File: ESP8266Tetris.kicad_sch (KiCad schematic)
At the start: 50 parts, among them J1 10118192-0001LF, Q1 BC847BLT1G, U2 STNS01PUR, U3 ESP-12F, U4 CH340G

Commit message: Battery charge and 3.3V LDO circuits changed, new datasheets added.
Signed-off-by: Ion Bold <bold.ion86@gmail.com>
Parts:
- removed C? (x3): 1u, symbol Device:C_Small
- removed C?: 2u2, symbol Device:C_Small
- removed C?: 4u7, symbol Device:C_Small
- removed R?: 10k, symbol Device:R_Small
- removed R?: 3M3?, symbol Device:R_Small
- removed R?: 10M?, symbol Device:R_Small
- removed U2: STNS01PUR, KiCadCustom:DFN12L_3x3mm_P0.45_EP2.12x1.31mm, symbol KiCadCustom:STNS01
- removed U?: BU33SD5WG-TR, Package_TO_SOT_SMD:SOT-23-5_HandSoldering, symbol KiCadCustom:BU33SD5WG-TR
- added C?: 1u, symbol Device:C_Small
- added C? (x2): 10u, symbol Device:C_Polarized_Small
- added R? (x2): 10k, symbol Device:R_Small
- added R?: 470R, symbol Device:R_Small
- added U?: LP3874EMPX-3.3/NOPB, Package_TO_SOT_SMD:SOT-223-5, symbol KiCadCustom:LP3874
- added U?: BQ25170, Package_SON:WSON-8-1EP_2x2mm_P0.5mm_EP0.9x1.6mm_ThermalVias, symbol KiCadCustom:BQ25170
- C1: value 2u2 -> 1u
- R1: value 1k -> 27k
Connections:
- net LED_EN is gone; now on net ROTATE: R?.2, U3.16 (GPIO15)
- net +3V3: now also C?.1, C?.2, Q?.2 (S), R?.1, R?.1, R?.1, R?.1, R?.1, U3.8 (VCC), C?.1, U?.3 (OUT), U?.4 (SENSE)
- net +5V: now also D?.2 (A), R?.2, U?.1 (IN)
- net BAT: now also BT?.1 (+), C?.1, C?.1, U?.2 (IN), U?.8 (OUT)
- net GND: now also C?.2, C?.2, C?.2, R?.2, R?.2, U?.4 (GND), U?.5 (GND)
- net ROTATE: no longer R?.2, U3.17 (GPIO2)
- net SD: now also R?.2, U3.17 (GPIO2), U?.1 (~{SD})
- net at R1.1: now also U?.7 (VSET)
- removed net +3V0: C?.1, C?.2, D?.2 (A), Q?.2 (S), R?.1, R?.1, R?.1, R?.1, R?.1, U3.8 (VCC)
- net LED_CHG: no longer names the net of R?.1
- net LED_CHG: now also U?.5 (STAT)
- new net: R?.1, U?.6 (~{PG})
- new net: R?.1, U?.2 (ISET)
- new net: R?.1, U?.3 (TS)
- no-connect marks 13 -> 12
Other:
- note added: "Condensatori tantal!!"
- note added: "PullDown resistors on buttons??"
- moved on the sheet: BT?, C1, D?, R1, R?

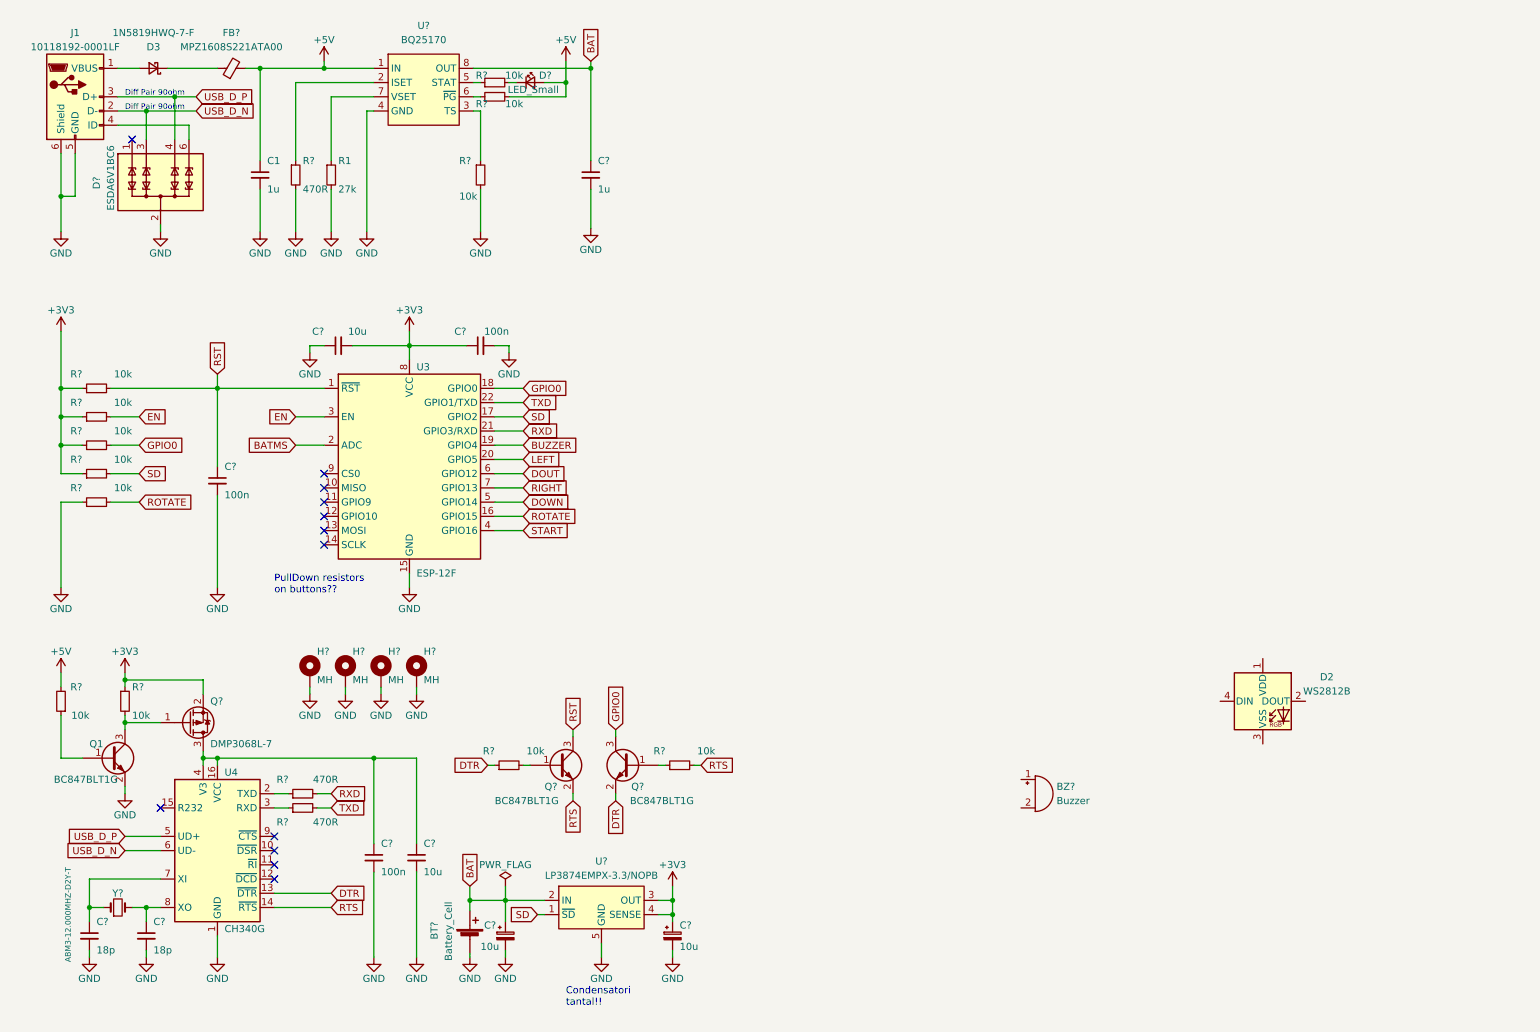
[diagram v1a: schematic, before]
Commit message: LEDs added to schematic, footprints assigned, PCB layout started.
Signed-off-by: Ion Bold <bold.ion86@gmail.com>
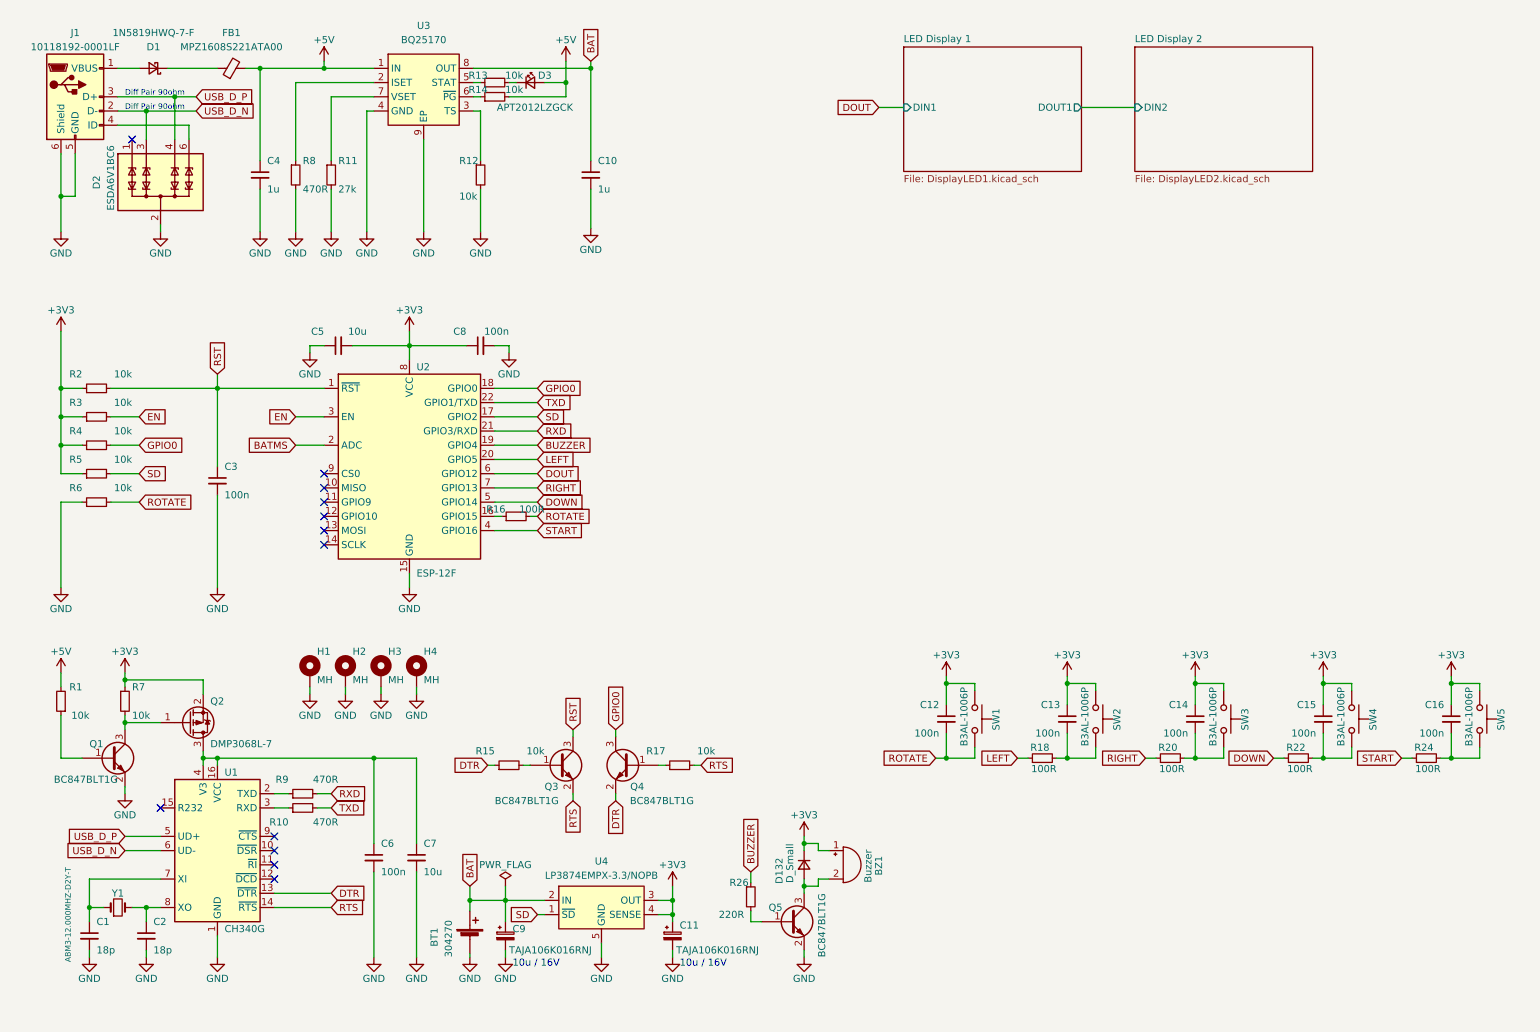
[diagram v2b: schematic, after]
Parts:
- removed D2: WS2812B, LED_SMD:LED_WS2812B_PLCC4_5.0x5.0mm_P3.2mm, symbol LED:WS2812B
- added C12, C13, C14, C15, C16: 100n, Capacitor_SMD:C_0603_1608Metric_Pad1.08x0.95mm_HandSolder, symbol Device:C_Small
- added D132: D_Small, Diode_SMD:D_MiniMELF, symbol Device:D_Small
- added Q5: BC847BLT1G, Package_TO_SOT_SMD:SOT-23, symbol Transistor_BJT:BC847
- added R16, R18, R20, R22, R24: 100R, Resistor_SMD:R_0603_1608Metric_Pad0.98x0.95mm_HandSolder, symbol Device:R_Small
- added R26: 220R, Resistor_SMD:R_0603_1608Metric_Pad0.98x0.95mm_HandSolder, symbol Device:R_Small
- added SW1, SW2, SW3, SW4, SW5: B3AL-1006P, KiCadCustom:SW_SPST_Omron_B3AL-100xP, symbol Switch:SW_Push
- BT1: renamed from BT?; value Battery_Cell -> 304270; footprint (none) -> KiCadCustom:Battery_LiPo_304270
- BZ1: renamed from BZ?; footprint (none) -> KiCadCustom:BUZZER_SMD
- C1, C10, C2, C3, C5, C6, C7, C8: renamed from C?; footprint (none) -> Capacitor_SMD:C_0603_1608Metric_Pad1.08x0.95mm_HandSolder
- C11, C9: renamed from C?; value 10u -> TAJA106K016RNJ; footprint (none) -> Capacitor_Tantalum_SMD:CP_EIA-3216-12_Kemet-S_Pad1.58x1.35mm_HandSolder
- C4: renamed from C1; footprint (none) -> Capacitor_SMD:C_0603_1608Metric_Pad1.08x0.95mm_HandSolder
- D3: renamed from D?; value LED_Small -> APT2012LZGCK; footprint (none) -> LED_SMD:LED_0805_2012Metric_Pad1.15x1.40mm_HandSolder
- FB1: renamed from FB?; footprint (none) -> Inductor_SMD:L_0603_1608Metric_Pad1.05x0.95mm_HandSolder
- H1, H2, H3, H4: renamed from H?; footprint (none) -> MountingHole:MountingHole_3.2mm_M3_DIN965_Pad
- R1, R10, R12, R13, R14, R15, R17, R2, R3, R4, R5, R6, R7, R8, R9: renamed from R?; footprint (none) -> Resistor_SMD:R_0603_1608Metric_Pad0.98x0.95mm_HandSolder
- R11: renamed from R1; footprint (none) -> Resistor_SMD:R_0603_1608Metric_Pad0.98x0.95mm_HandSolder
- Y1: renamed from Y?; footprint (none) -> Crystal:Crystal_SMD_7050-2Pin_7.0x5.0mm_HandSoldering
- gave numbers to parts that had none: 6
- renumbered D3 to D1, U4 to U1, U3 to U2
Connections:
- net +3V3: now also BZ1.1 (-), C12.1, C13.1, C14.1, C15.1, C16.1, D132.1 (K), SW1.1, SW2.1, SW3.1, SW4.1, SW5.1
- net BUZZER: now also R26.1
- net DOWN: now also R22.1
- net GND: now also U3.9 (EP), Q5.2 (E)
- net LEFT: now also R18.1
- net RIGHT: now also R20.1
- net ROTATE: now also C12.2, R16.2, SW1.2; no longer U2.16 (GPIO15)
- net START: now also R24.1
- net at BZ1.2 (+): now also D132.2 (A), Q5.3 (C)
- new net: C16.2, R24.2, SW5.2
- new net: C15.2, R22.2, SW4.2
- new net: Q5.1 (B), R26.2
- new net: C13.2, R18.2, SW2.2
- new net: C14.2, R20.2, SW3.2
- new net: R16.1, U2.16 (GPIO15)
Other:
- added sheet LED Display 1 (DisplayLED1.kicad_sch)
- added sheet LED Display 2 (DisplayLED2.kicad_sch)
- note added: "10u / 16V"
- note removed: "Condensatori tantal!!"
- note removed: "PullDown resistors on buttons??"
- moved on the sheet: BZ1

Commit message: Soft letching power switch circuit added, buttons reassigned to GPIOs.
Signed-off-by: Ion Bold <bold.ion86@gmail.com>
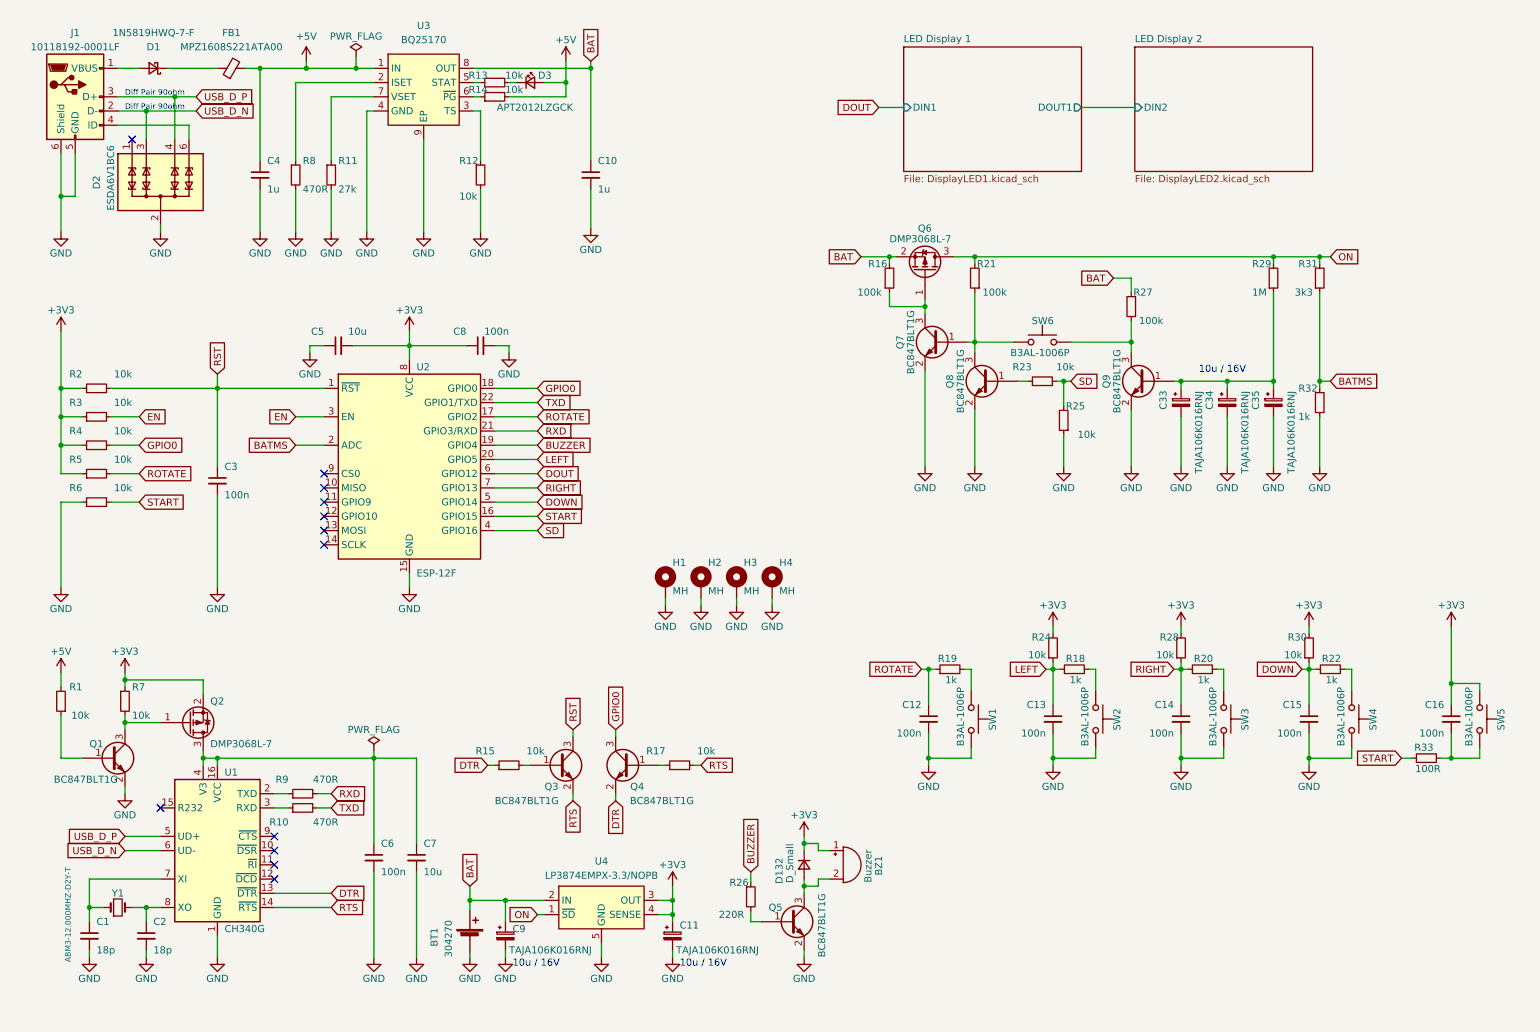
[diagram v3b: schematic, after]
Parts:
- added C33, C34, C35: TAJA106K016RNJ, Capacitor_Tantalum_SMD:CP_EIA-3216-12_Kemet-S_Pad1.58x1.35mm_HandSolder, symbol Device:C_Polarized_Small
- added Q6: DMP3068L-7, Package_TO_SOT_SMD:SOT-23, symbol Transistor_FET:DMG2301L
- added Q7, Q8, Q9: BC847BLT1G, Package_TO_SOT_SMD:SOT-23, symbol Transistor_BJT:BC847
- added R19, R32: 1k, Resistor_SMD:R_0603_1608Metric_Pad0.98x0.95mm_HandSolder, symbol Device:R_Small
- added R21, R27: 100k, Resistor_SMD:R_0603_1608Metric_Pad0.98x0.95mm_HandSolder, symbol Device:R_Small
- added R23, R25, R28, R30: 10k, Resistor_SMD:R_0603_1608Metric_Pad0.98x0.95mm_HandSolder, symbol Device:R_Small
- added R29: 1M, Resistor_SMD:R_0603_1608Metric_Pad0.98x0.95mm_HandSolder, symbol Device:R_Small
- added R31: 3k3, Resistor_SMD:R_0603_1608Metric_Pad0.98x0.95mm_HandSolder, symbol Device:R_Small
- added R33: 100R, Resistor_SMD:R_0603_1608Metric_Pad0.98x0.95mm_HandSolder, symbol Device:R_Small
- added SW6: B3AL-1006P, KiCadCustom:SW_SPST_Omron_B3AL-100xP, symbol Switch:SW_Push
- R16: value 100R -> 100k
- R18, R20, R22: value 100R -> 1k
- R24: value 100R -> 10k
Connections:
- net +3V3: now also R24.2, R28.2, R30.2; no longer C12.1, C13.1, C14.1, C15.1, SW1.1, SW2.1, SW3.1, SW4.1
- net BAT: now also R16.2, Q6.2 (S), R27.2
- net BATMS: now also R31.1, R32.2
- net DOWN: now also C15.1, R30.1
- net GND: now also C12.2, C13.2, C14.2, C15.2, SW1.2, SW2.2, SW3.2, SW4.2, C33.2, C34.2, C35.2, Q7.2 (E), Q8.2 (E), Q9.2 (E), R25.1, R32.1
- net LEFT: now also C13.1, R24.1
- net RIGHT: now also C14.1, R28.1
- net ROTATE: now also C12.1, R5.2, U2.17 (GPIO2), R19.1; no longer C12.2, R16.2, R6.2, SW1.2
- net SD: now also U2.4 (GPIO16), R23.2, R25.2; no longer R5.2, U2.17 (GPIO2), U4.1 (~{SD})
- net START: now also R6.2, U2.16 (GPIO15), R33.1; no longer R24.1, U2.4 (GPIO16)
- net at C16.2, SW5.2: now also R33.2; no longer R24.2
- net at R16.1: now also Q6.1 (G), Q7.3 (C); no longer U2.16 (GPIO15)
- new net: R22.2, SW4.1
- new net: C33.1, C34.1, C35.1, Q9.1 (B), R29.1
- new net: Q9.3 (C), R27.1, SW6.2
- new net: R19.2, SW1.1
- new net: R20.2, SW3.1
- new net: Q7.1 (B), Q8.3 (C), R21.1, SW6.1
- new net: R18.2, SW2.1
- new net: Q8.1 (B), R23.1
- new net ON: Q6.3 (D), R21.2, R29.2, R31.2, U4.1 (~{SD})
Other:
- moved on the sheet: C12, C13, C14, C15, H1, H2, H3, H4, R18, R20, R22, SW1

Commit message: Schematic finished, routing PCB started.
Signed-off-by: Ion Bold <bold.ion86@gmail.com>
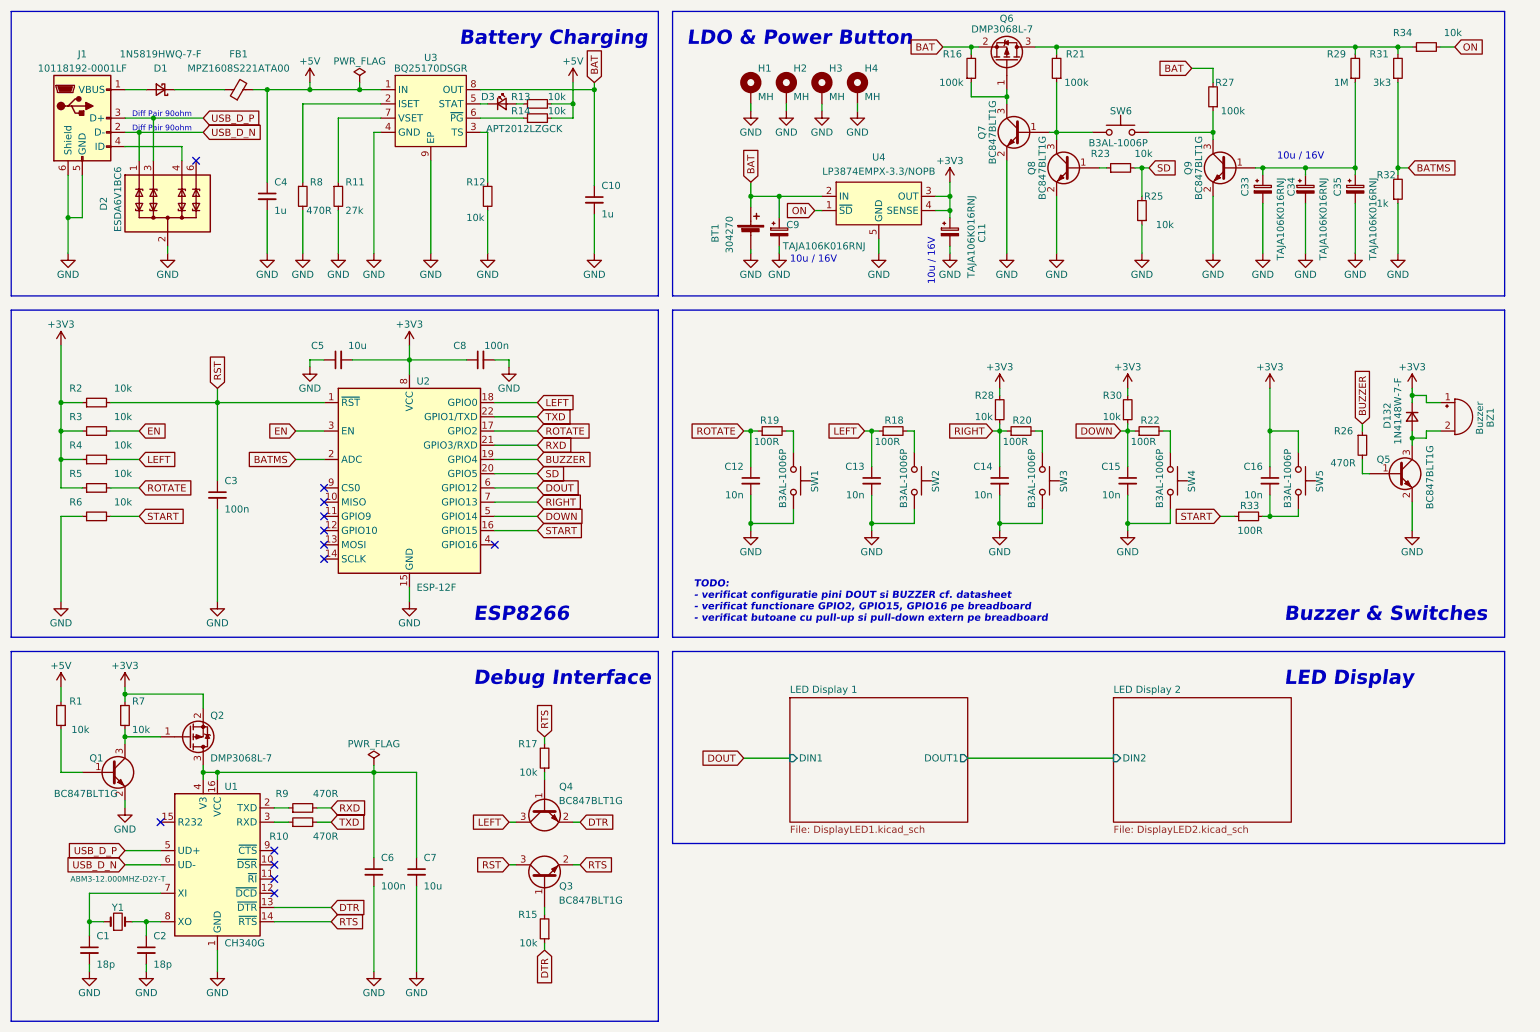
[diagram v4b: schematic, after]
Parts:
- removed R24: 10k, Resistor_SMD:R_0603_1608Metric_Pad0.98x0.95mm_HandSolder, symbol Device:R_Small
- added R34: 10k, Resistor_SMD:R_0603_1608Metric_Pad0.98x0.95mm_HandSolder, symbol Device:R_Small
- C12, C13, C14, C15, C16: value 100n -> 10n
- D132: value D_Small -> 1N4148W-7-F; footprint Diode_SMD:D_MiniMELF -> Diode_SMD:D_SOD-123
- R18, R19, R20, R22: value 1k -> 100R
- R26: value 220R -> 470R
- U3: value BQ25170 -> BQ25170DSGR
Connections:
- net GPIO0 is gone; now on net LEFT: Q4.3 (C), R4.2, U2.18 (GPIO0)
- net +5V: now also R13.2; no longer D3.2 (A)
- net LEFT: no longer U2.20 (GPIO5)
- net ON: now also R34.2; no longer Q6.3 (D), R21.2, R29.2, R31.2
- net SD: now also U2.20 (GPIO5); no longer U2.4 (GPIO16)
- net USB_D_N: now also D2.1 (TVS1); no longer D2.3 (TVS2)
- net USB_D_P: now also D2.3 (TVS2); no longer D2.4 (TVS3)
- net at J1.4 (ID): now also D2.4 (TVS3); no longer D2.6 (TVS4)
- net at U3.5 (STAT): now also D3.1 (K); no longer R13.1
- new net: Q6.3 (D), R21.2, R29.2, R31.2, R34.1
- new net: D3.2 (A), R13.1
- no-connect marks 12 -> 13
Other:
- note added: "Battery Charging"
- note added: "Buzzer & Switches"
- note added: "Debug Interface"
- note added: "ESP8266"
- note added: "LDO & Power Button"
- note added: "LED Display"
- note added: "TODO: - verificat configuratie pini DOUT si BUZZER cf. datasheet - verificat functionare GPIO2, GPIO15, GPIO16 pe breadboard - verificat butoane cu pull-up si pull-down extern pe breadboard"
- moved on the sheet: BT1, BZ1, C1, C10, C11, C12, C13, C14, C15, C16, C2, C3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
